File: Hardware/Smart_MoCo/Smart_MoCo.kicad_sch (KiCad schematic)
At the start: 40 parts, among them J1 Conn_01x04, J2 Conn_01x05, U1 STM32F042F6Px, U2 VNH5019A-E, U3 ATA6561

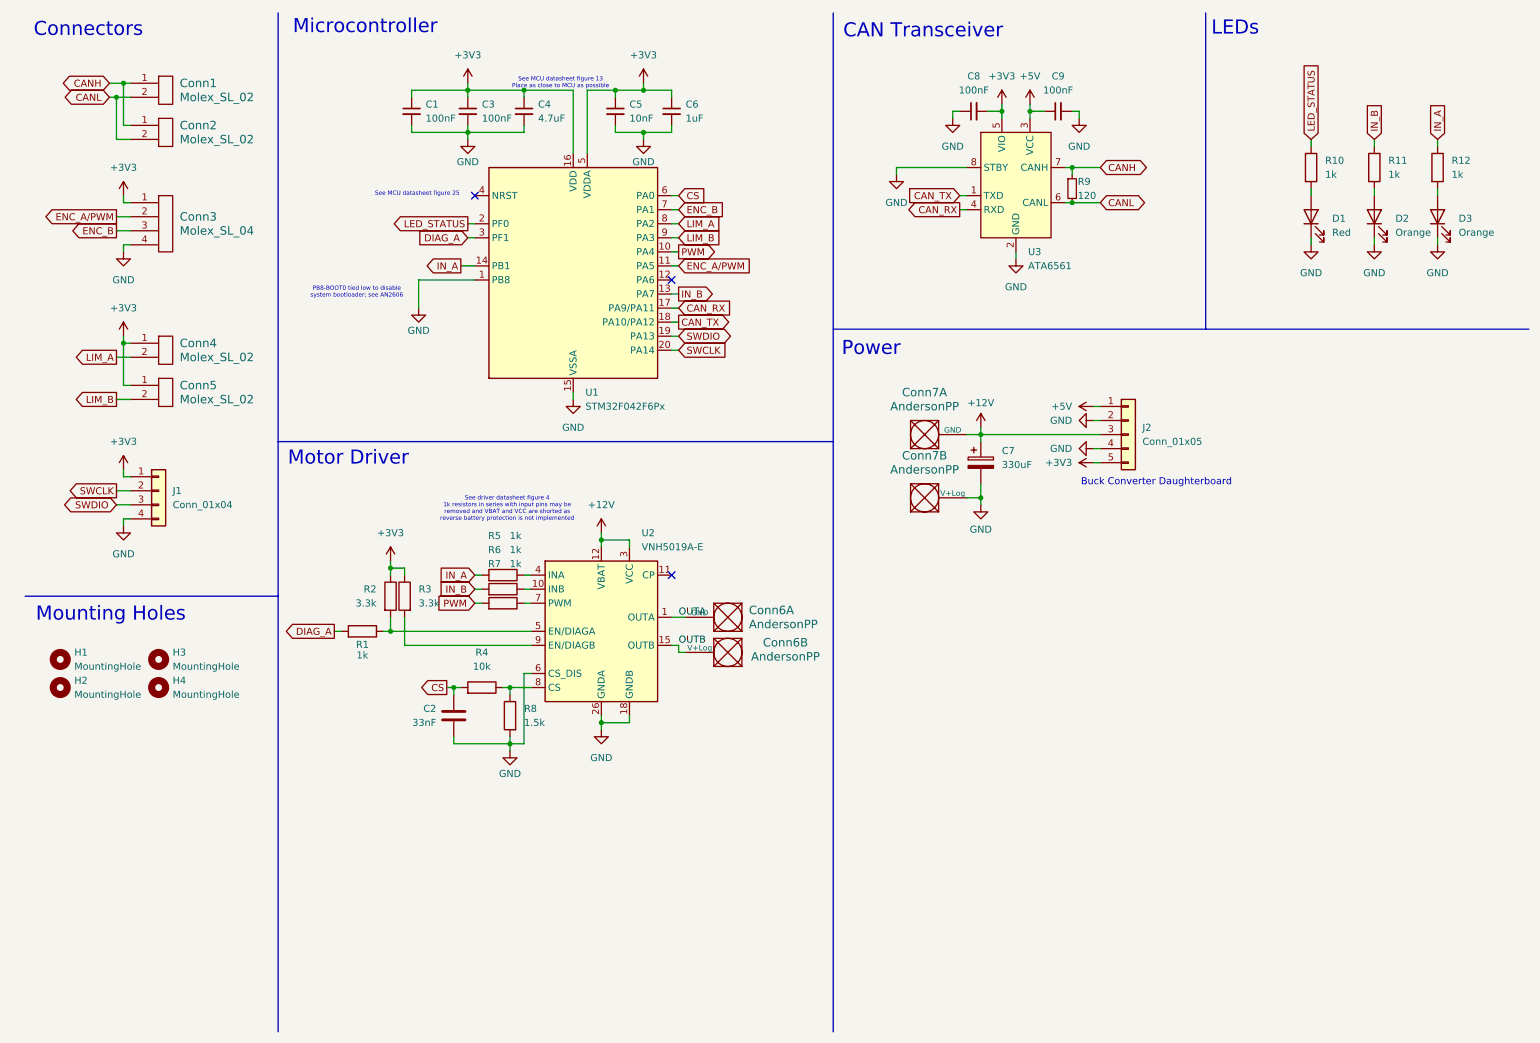
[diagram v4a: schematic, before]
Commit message: Change power connectors, increase layer count to 4, and reroute
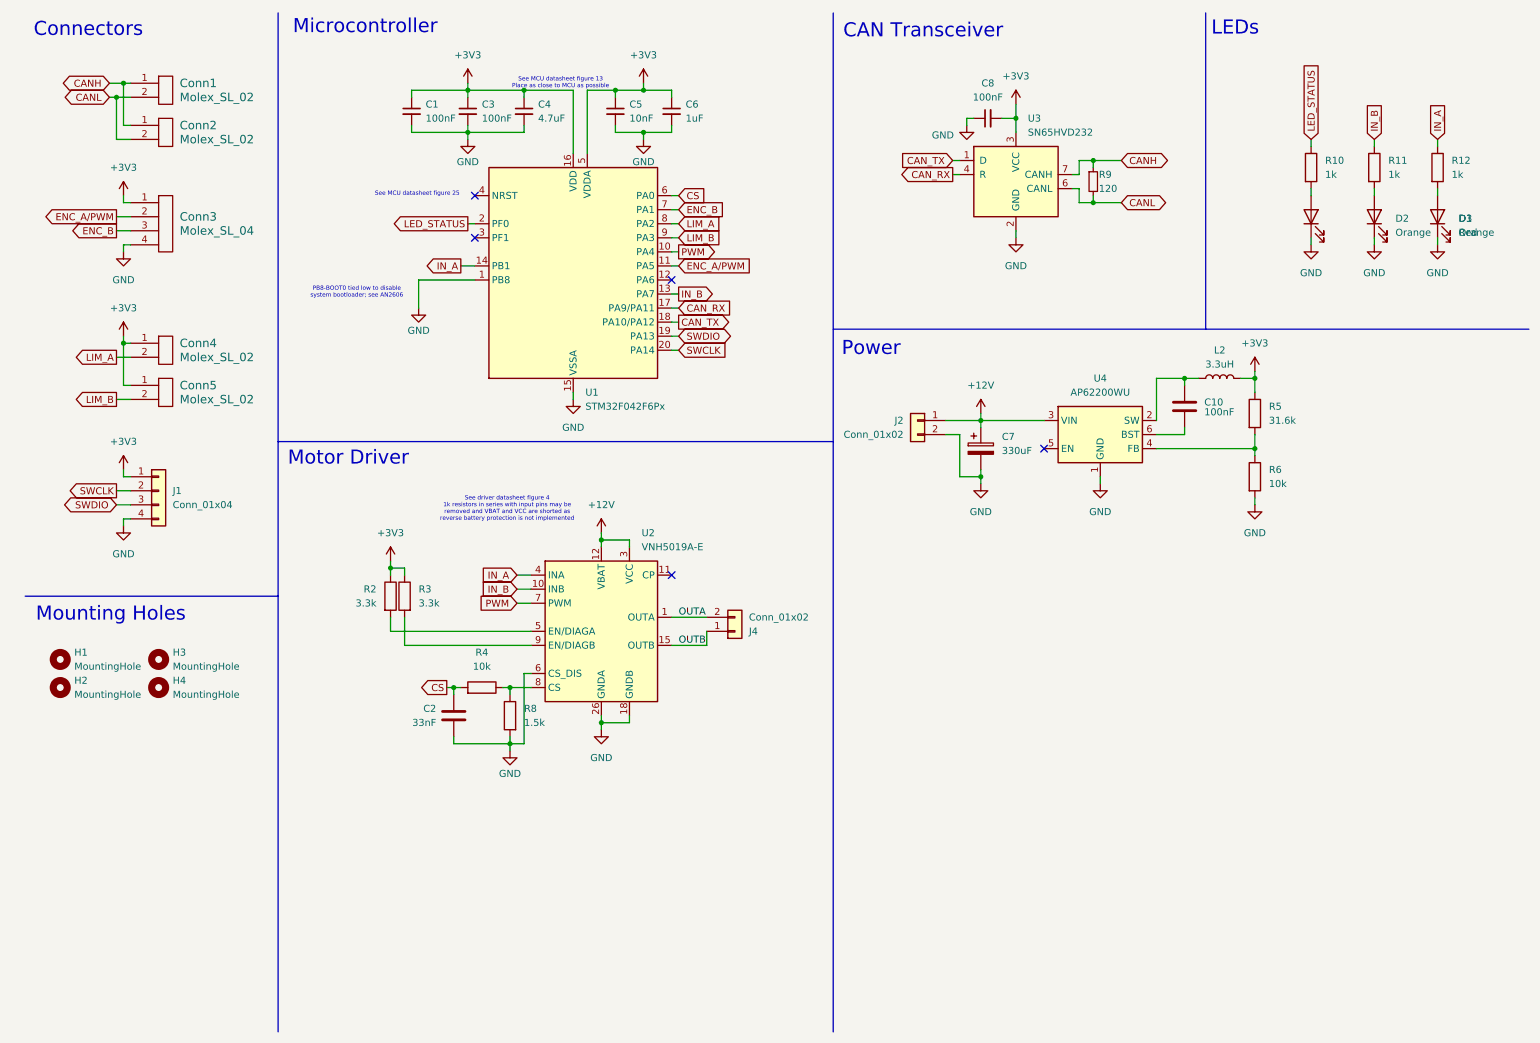
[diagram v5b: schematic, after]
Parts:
- removed C9: 100nF, Capacitor_SMD:C_0603_1608Metric_Pad1.08x0.95mm_HandSolder, symbol Device:C_Small
- removed Conn6, Conn7: AndersonPP, Local Libraries:Square_Anderson_2_V_Side_By_Side_No_Silkscreen, symbol MRDT_Connectors:AndersonPP
- removed J2: Conn_01x05, Connector_PinSocket_2.54mm:PinSocket_1x05_P2.54mm_Vertical, symbol Connector_Generic:Conn_01x05
- removed R1, R7: 1k, Resistor_SMD:R_0603_1608Metric_Pad0.98x0.95mm_HandSolder, symbol Device:R
- removed U3: ATA6561, Package_SO:SOIC-8_3.9x4.9mm_P1.27mm, symbol MRDT_Devices:ATA6561
- added C10: 100nF, Capacitor_SMD:C_0603_1608Metric_Pad1.08x0.95mm_HandSolder, symbol Device:C
- added J2, J4: Conn_01x02, Connector_Molex:Molex_Mega-Fit_76829-0102_2x01_P5.70mm_Vertical, symbol Connector_Generic:Conn_01x02
- added L2: 3.3uH, Inductor_SMD:L_1008_2520Metric_Pad1.43x2.20mm_HandSolder, symbol Device:L
- added U3: SN65HVD232, Package_SO:SOIC-8_3.9x4.9mm_P1.27mm, symbol Interface_CAN_LIN:SN65HVD232
- added U4: AP62200WU, Package_TO_SOT_SMD:TSOT-23-6, symbol Regulator_Switching:AP62250WU
- R5: value 1k -> 31.6k
- R6: value 1k -> 10k
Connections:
- net +12V: now also J2.1 (Pin_1), U4.3 (VIN)
- net +3V3: now also R5.1, L2.2, U3.3 (VCC)
- net CANH: now also U3.7 (CANH)
- net CANL: now also U3.6 (CANL)
- net CAN_RX: now also U3.4 (R)
- net CAN_TX: now also U3.1 (D)
- net GND: now also R6.2, J2.2 (Pin_2), U3.2 (GND), U4.1 (GND)
- net IN_A: now also U2.4 (INA); no longer R5.2
- net IN_B: now also U2.10 (INB); no longer R6.2
- net OUTA: now also J4.2 (Pin_2)
- net OUTB: now also J4.1 (Pin_1)
- net PWM: now also U2.7 (PWM)
- net at R6.1: now also R5.2, U4.4 (FB); no longer U2.10 (INB)
- net DIAG_A: no longer names the net of U1.3 (PF1)
- new net: C10.1, L2.1, U4.2 (SW)
- new net: C10.2, U4.6 (BST)
- no-connect marks 3 -> 5
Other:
- note removed: "Buck Converter Daughterboard"
- moved on the sheet: C7, C8, R9

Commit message: Change power connectors again
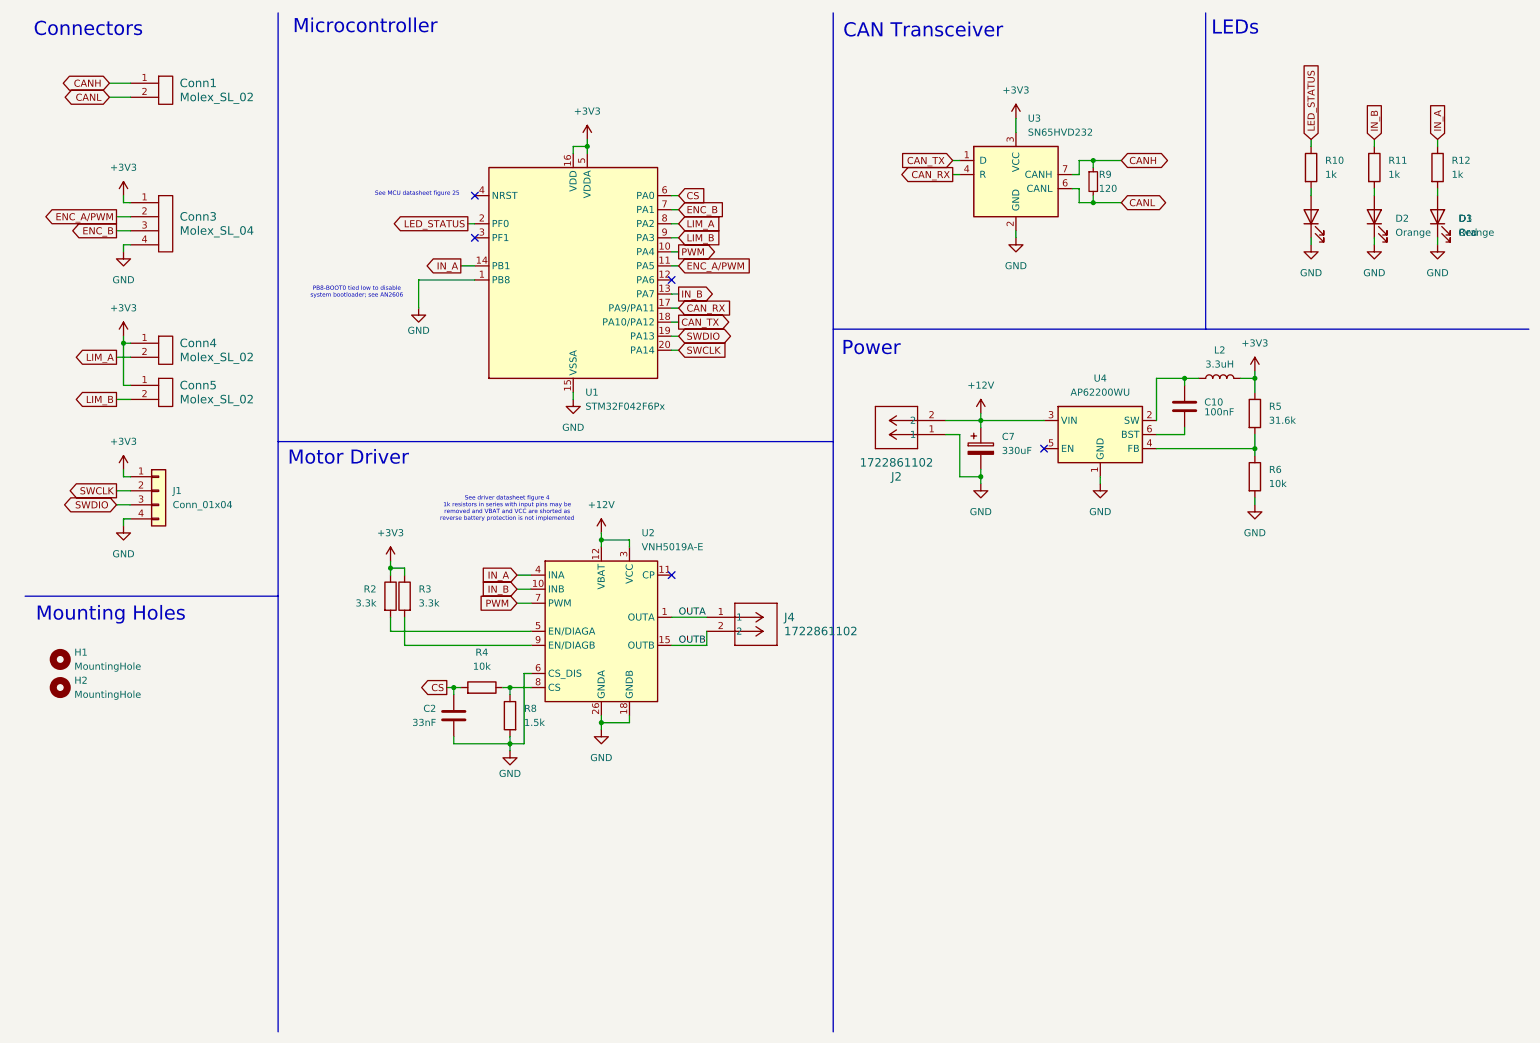
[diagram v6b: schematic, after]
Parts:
- removed C1, C3, C8: 100nF, Capacitor_SMD:C_0603_1608Metric_Pad1.08x0.95mm_HandSolder, symbol Device:C_Small
- removed C4: 4.7uF, Capacitor_SMD:C_0603_1608Metric_Pad1.08x0.95mm_HandSolder, symbol Device:C_Small
- removed C5: 10nF, Capacitor_SMD:C_0603_1608Metric_Pad1.08x0.95mm_HandSolder, symbol Device:C_Small
- removed C6: 1uF, Capacitor_SMD:C_0603_1608Metric_Pad1.08x0.95mm_HandSolder, symbol Device:C_Small
- removed Conn2: Molex_SL_02, MRDT_Connectors:MOLEX_SL_02_Vertical, symbol MRDT_Connectors:Molex_SL_02
- removed H3, H4: MountingHole, MRDT_Drill_Holes:4_40_Hole, symbol Mechanical:MountingHole
- removed J2, J4: Conn_01x02, Connector_Molex:Molex_Mega-Fit_76829-0102_2x01_P5.70mm_Vertical, symbol Connector_Generic:Conn_01x02
- added J2, J4: 1722861102, MRDT_Connectors:CONN_SD-172286-1000_02_MOL, symbol MRDT_Connectors:1722861102
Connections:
- net +12V: now also J2.2
- net GND: now also J2.1
- net OUTA: now also J4.1
- net OUTB: now also J4.2
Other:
- note removed: "See MCU datasheet figure 13 Place as close to MCU as possible"

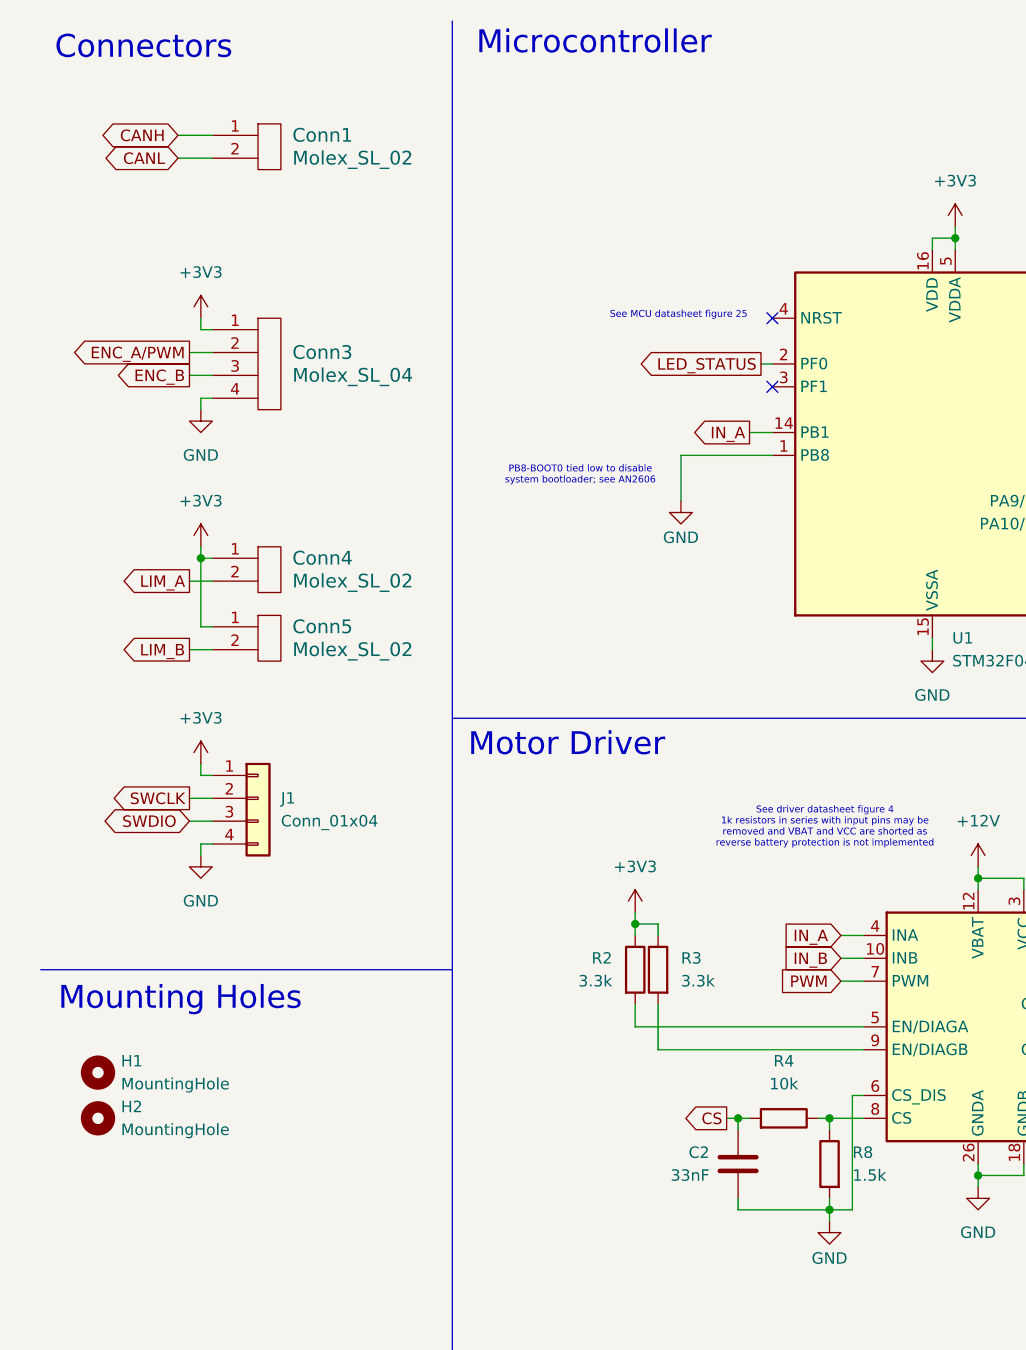
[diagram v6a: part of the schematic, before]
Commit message: Change signal connectors to horizontal JST SH
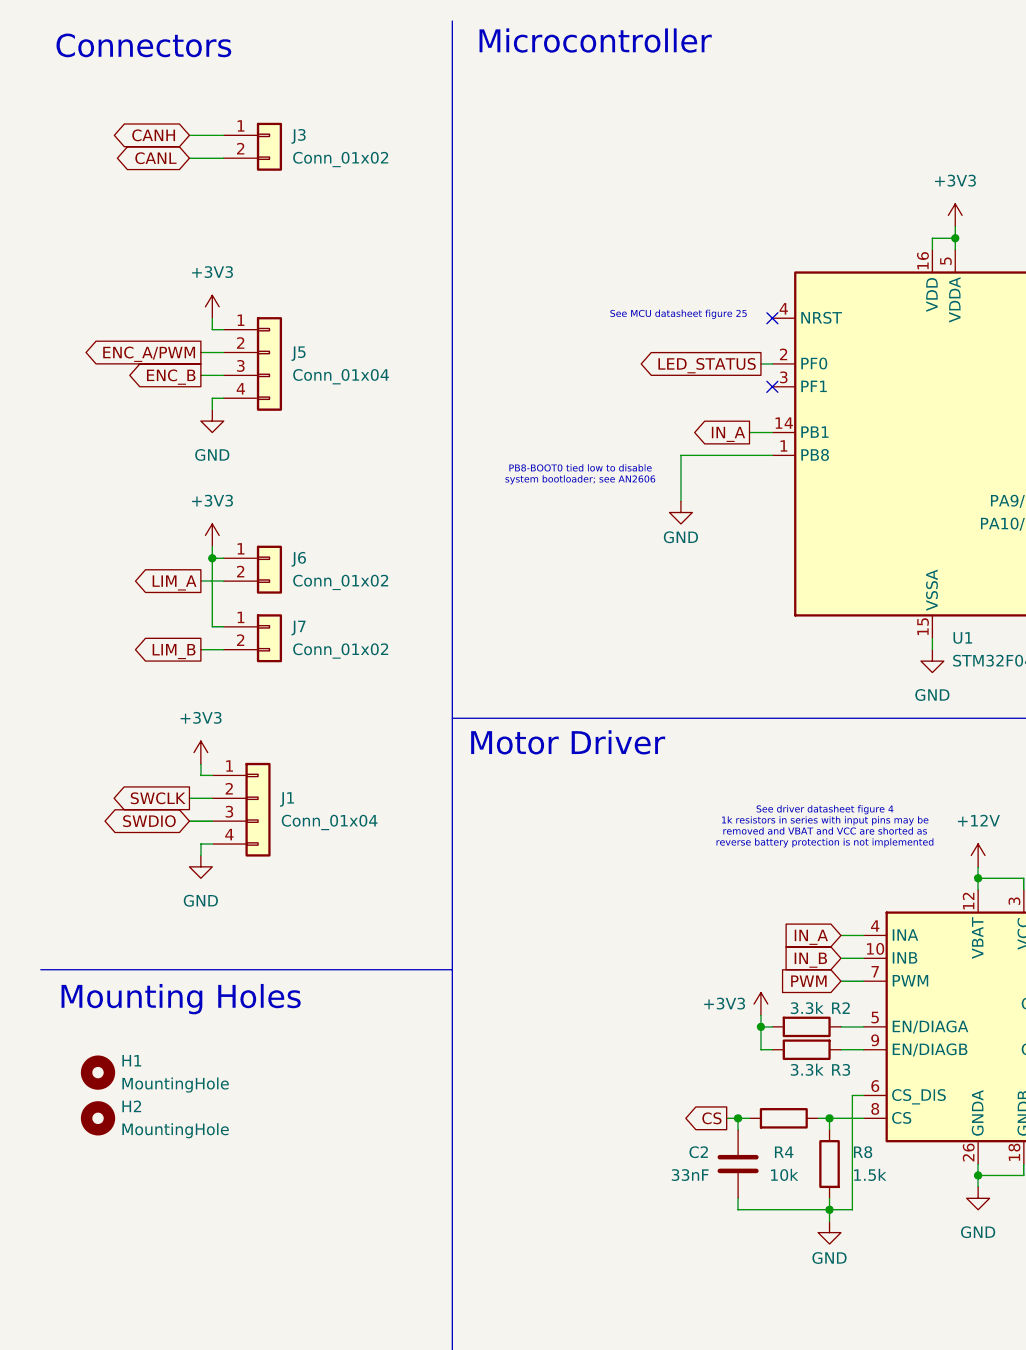
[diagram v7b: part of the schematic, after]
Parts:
- removed Conn1, Conn4, Conn5: Molex_SL_02, MRDT_Connectors:MOLEX_SL_02_Vertical, symbol MRDT_Connectors:Molex_SL_02
- removed Conn3: Molex_SL_04, MRDT_Connectors:MOLEX_SL_04_Vertical, symbol MRDT_Connectors:Molex_SL_04
- added J3, J6, J7: Conn_01x02, Connector_JST:JST_SH_SM02B-SRSS-TB_1x02-1MP_P1.00mm_Horizontal, symbol Connector_Generic:Conn_01x02
- added J5: Conn_01x04, Connector_JST:JST_SH_SM04B-SRSS-TB_1x04-1MP_P1.00mm_Horizontal, symbol Connector_Generic:Conn_01x04
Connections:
- net +3V3: now also R2.2, J5.1 (Pin_1), J6.1 (Pin_1), J7.1 (Pin_1); no longer R2.1
- net CANH: now also J3.1 (Pin_1)
- net CANL: now also J3.2 (Pin_2)
- net ENC_A/PWM: now also J5.2 (Pin_2)
- net ENC_B: now also J5.3 (Pin_3)
- net GND: now also J5.4 (Pin_4)
- net LIM_A: now also J6.2 (Pin_2)
- net LIM_B: now also J7.2 (Pin_2)
- net at U2.5 (EN/DIAGA): now also R2.1; no longer R2.2
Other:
- moved on the sheet: R2, R3

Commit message: Shrink board to 27x40mm
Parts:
- H1, H2: footprint MRDT_Drill_Holes:4_40_Hole -> Local Libraries:Minimal_4_40_Hole
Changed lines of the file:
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@@
 			)
 		)
-		(property "Footprint" "MRDT_Drill_Holes:4_40_Hole"
+		(property "Footprint" "Local Libraries:Minimal_4_40_Hole"
 			(at 19.05 129.54 0)
 			(effects
@@
 			)
 		)
-		(property "Footprint" "MRDT_Drill_Holes:4_40_Hole"
+		(property "Footprint" "Local Libraries:Minimal_4_40_Hole"
 			(at 19.05 134.62 0)
 			(effects
